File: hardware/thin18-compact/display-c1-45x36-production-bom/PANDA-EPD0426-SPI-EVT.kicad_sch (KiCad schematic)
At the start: 37 parts, among them J1 DF40C-60DP-0.4V(51), J2 FH12-24S-0.5SH(55), Q1 NX3008NBK,215, U1 AIP74LVC2G17GC363.TR, U2 AIP74LVC2G17GC363.TR, U3 AIP74LVC2G17GC363.TR

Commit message: feat(hw): audit split stack and verify exact-part sourcing
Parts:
- C10: LCSC (none) -> C77080
- C11, C12, C13: LCSC (none) -> C77050
- C4, C5, C6, C7, C8, C9: LCSC (none) -> C77077
- D1, D2, D3: LCSC (none) -> C82046
- J1: LCSC (none) -> C424647
- J2: LCSC (none) -> C202112
- Q1: LCSC (none) -> C179399
- R1, R2, R3, R4, R5: LCSC (none) -> C114765
- R13: LCSC (none) -> C112307
- R6: LCSC (none) -> C106232

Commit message: hw: apply reviewed domestic ECOs and gate incomplete Split-C1 orders
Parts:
- C10: LCSC C77080 -> C89190; MPN GRM21BR71E105KA99L -> 0805B105K250NT; Manufacturer Murata -> FH (Fenghua Advanced)
- C11, C12, C13: LCSC C77050 -> C694249; MPN GRM188R71E104KA01D -> 0603B104K250NT; Manufacturer Murata -> FH (Fenghua Advanced)
- C4, C5, C6, C7, C8, C9: value 4.7u 25V X5R -> 4.7u 25V X7R; LCSC C77077 -> C37818; MPN GRM21BR61E475KA12L -> 0805B475K250NT; Manufacturer Murata -> FH (Fenghua Advanced)
- D1, D2, D3: value MBR0530T1G -> MBR0530; footprint Diode_SMD:D_SOD-123 -> panda-r6-display:MBR0530_JSCJ_SOD123; LCSC C82046 -> C77336; MPN MBR0530T1G -> MBR0530; Manufacturer onsemi -> JSCJ
- J1: value DF40C-60DP-0.4V(51) -> HC-PBB40C-60DP-0.4V-02; footprint Connector_Hirose_DF40:Hirose_DF40C-60DP-0.4V_2x30-1MP_P0.4mm -> panda-r6-display:HCTL_PBB40C_60DP_04V; LCSC C424647 -> C19089235; MPN DF40C-60DP-0.4V(51) -> HC-PBB40C-60DP-0.4V-02; Manufacturer Hirose -> HCTL
- R1, R2, R3, R4, R5: LCSC C114765 -> C324769; MPN RC0402FR-0722RL -> RC-02K22R0FT; Manufacturer YAGEO -> FH (Fenghua Advanced)
- R10, R11, R12, R7, R8, R9: LCSC C25741 -> C140219; MPN 0402WGF1003TCE -> RC-02K1003FT; Manufacturer UNI-ROYAL -> FH (Fenghua Advanced)
- R13: LCSC C112307 -> C322118; MPN RC0603FR-072R2L -> RS-03L2R20FT; Manufacturer YAGEO -> FH (Fenghua Advanced)
- R14: LCSC C25744 -> C140215; MPN 0402WGF1002TCE -> RC-02K1002FT; Manufacturer UNI-ROYAL -> FH (Fenghua Advanced)
- R6: LCSC C106232 -> C140217; MPN RC0402FR-07100RL -> RC-02K1000FT; Manufacturer YAGEO -> FH (Fenghua Advanced)

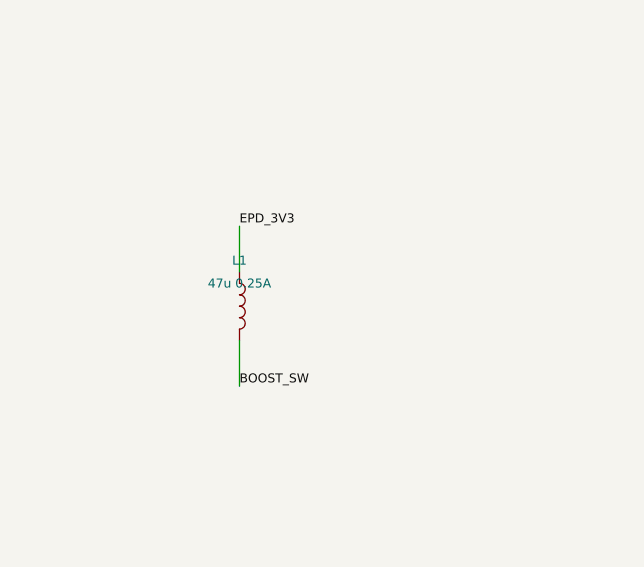
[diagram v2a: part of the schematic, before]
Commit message: hw: apply domestic wire, FPC and inductor ECOs with replay guards
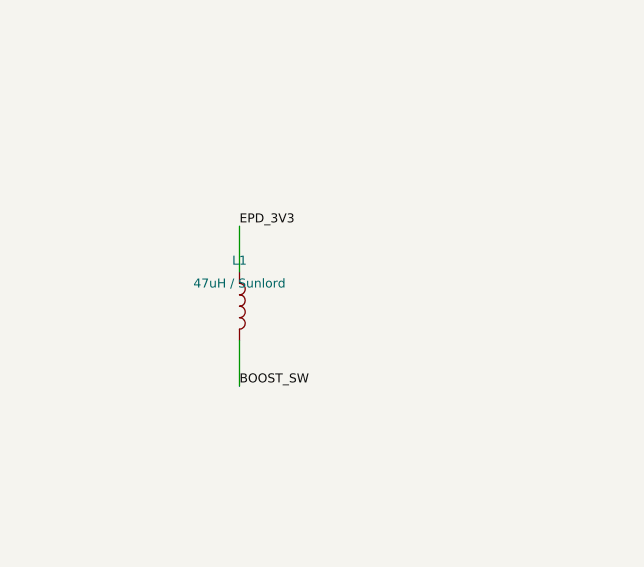
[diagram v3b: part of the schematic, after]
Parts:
- L1: value 47u 0.25A -> 47uH / Sunlord; footprint panda-r6-display:L_Taiyo_NRH3010_3030 -> panda-r6-display:Sunlord_SWPA3012_47u; MPN LSXNE3030KKT470MN -> SWPA3012S470MT; Manufacturer Taiyo Yuden -> Sunlord

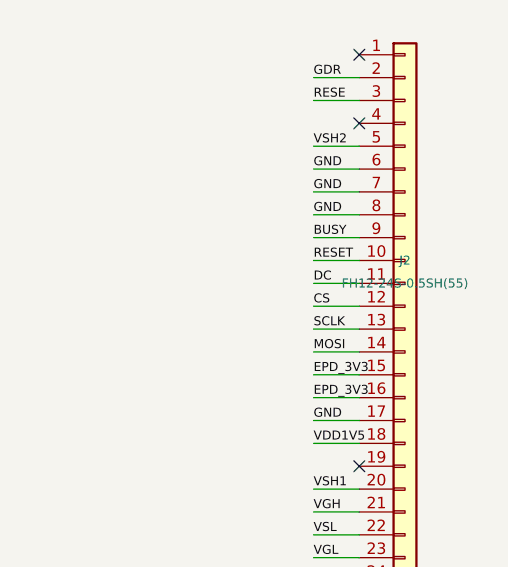
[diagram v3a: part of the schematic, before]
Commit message: hardware: close three imported Split-C1 refs and two SMT maps
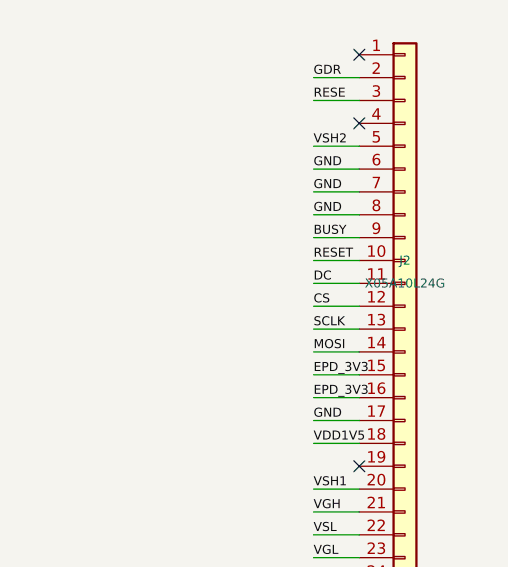
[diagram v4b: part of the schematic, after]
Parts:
- J2: value FH12-24S-0.5SH(55) -> X05A10L24G; footprint Connector_FFC-FPC:Hirose_FH12-24S-0.5SH_1x24-1MP_P0.50mm_Horizontal -> panda-r6-display:XKB_X05A10L24G; LCSC C202112 -> C2880917; MPN FH12-24S-0.5SH(55) -> X05A10L24G; Manufacturer Hirose -> XKB Connection
- L1: LCSC (none) -> C83420

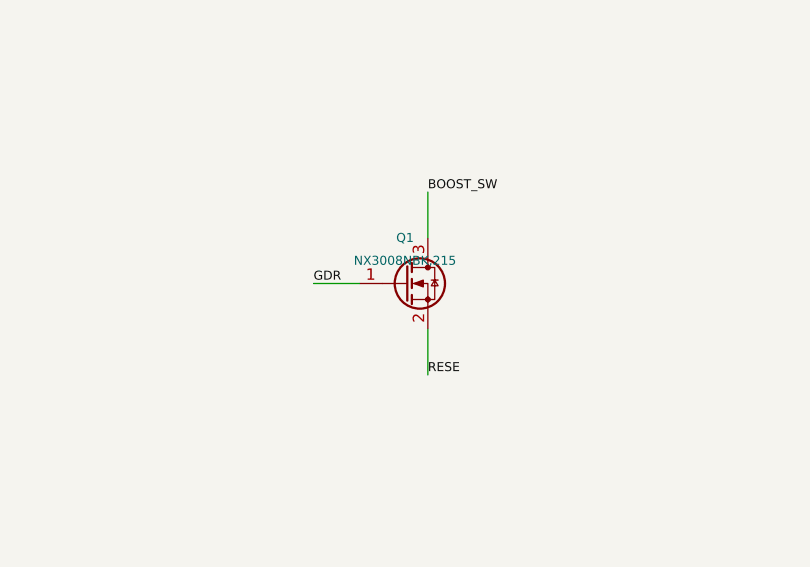
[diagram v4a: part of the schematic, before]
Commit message: hw: complete Split-C1 domestic RTC backup and EPD MOS ECO
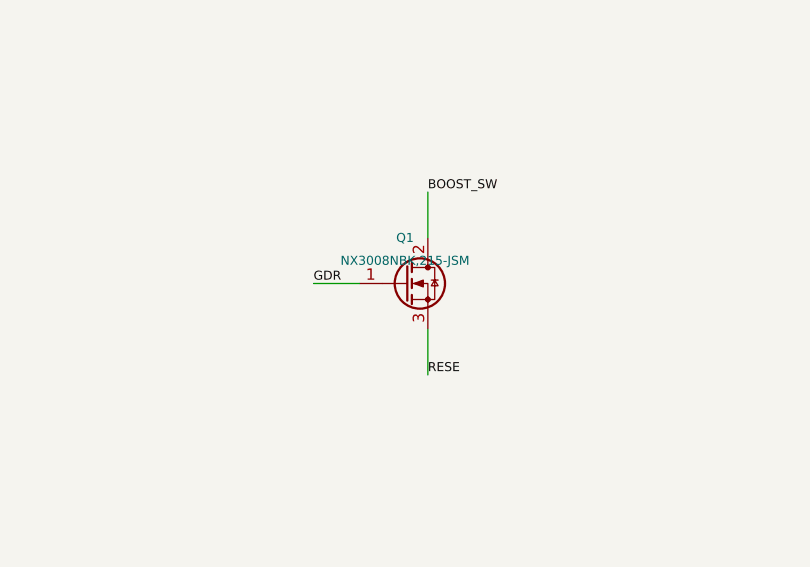
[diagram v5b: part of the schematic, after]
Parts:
- Q1: value NX3008NBK,215 -> NX3008NBK,215-JSM; footprint Package_TO_SOT_SMD:SOT-23 -> panda-r6-display:JSM_NX3008NBK_SOT23; symbol Transistor_FET:Q_NMOS_GSD -> panda-r6-display:NX3008NBK_215_JSM; LCSC C179399 -> C53113911; MPN NX3008NBK,215 -> NX3008NBK,215-JSM; Manufacturer Nexperia -> JSMSEMI
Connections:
- net BOOST_SW: now also Q1.2 (D); no longer Q1.3 (D)
- net RESE: now also Q1.3 (S); no longer Q1.2 (S)
